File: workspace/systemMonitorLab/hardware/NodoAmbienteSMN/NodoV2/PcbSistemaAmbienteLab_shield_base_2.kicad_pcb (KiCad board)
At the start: 2 copper layers, 55.1 x 66.3 mm, 18 parts, among them J1 Molex_MainBoard_DHT22, J2 Molex_MainBoard_BMP280, J3 Jack-DC, J6 Molex_MainBoard_Led_Status, Q1 Q_NPN_BEC, Q2 Q_NPN_BEC, Q3 Q_NPN_BEC, Q4 Q_NPN_BEC, U1 NodeMcuEsp8266

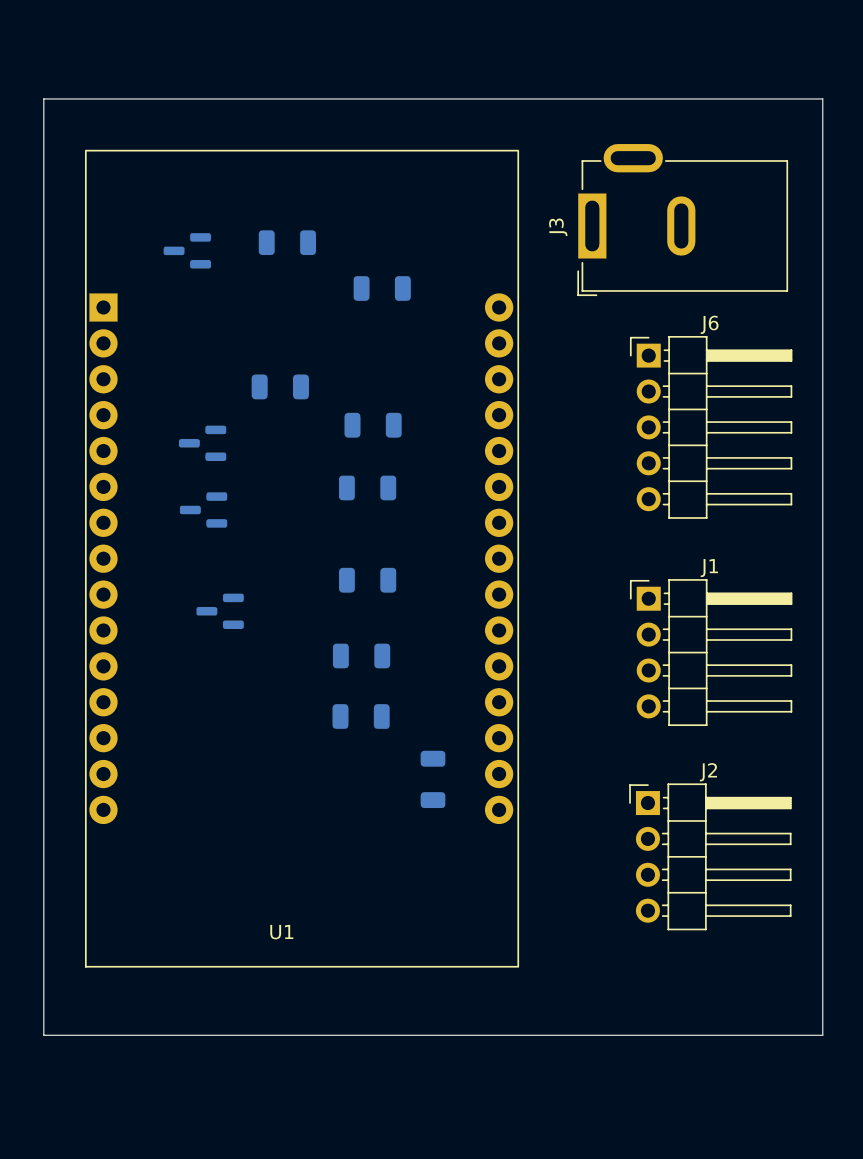
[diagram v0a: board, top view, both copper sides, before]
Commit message: Se termino de generar el diseño de la placa shield_main_board.
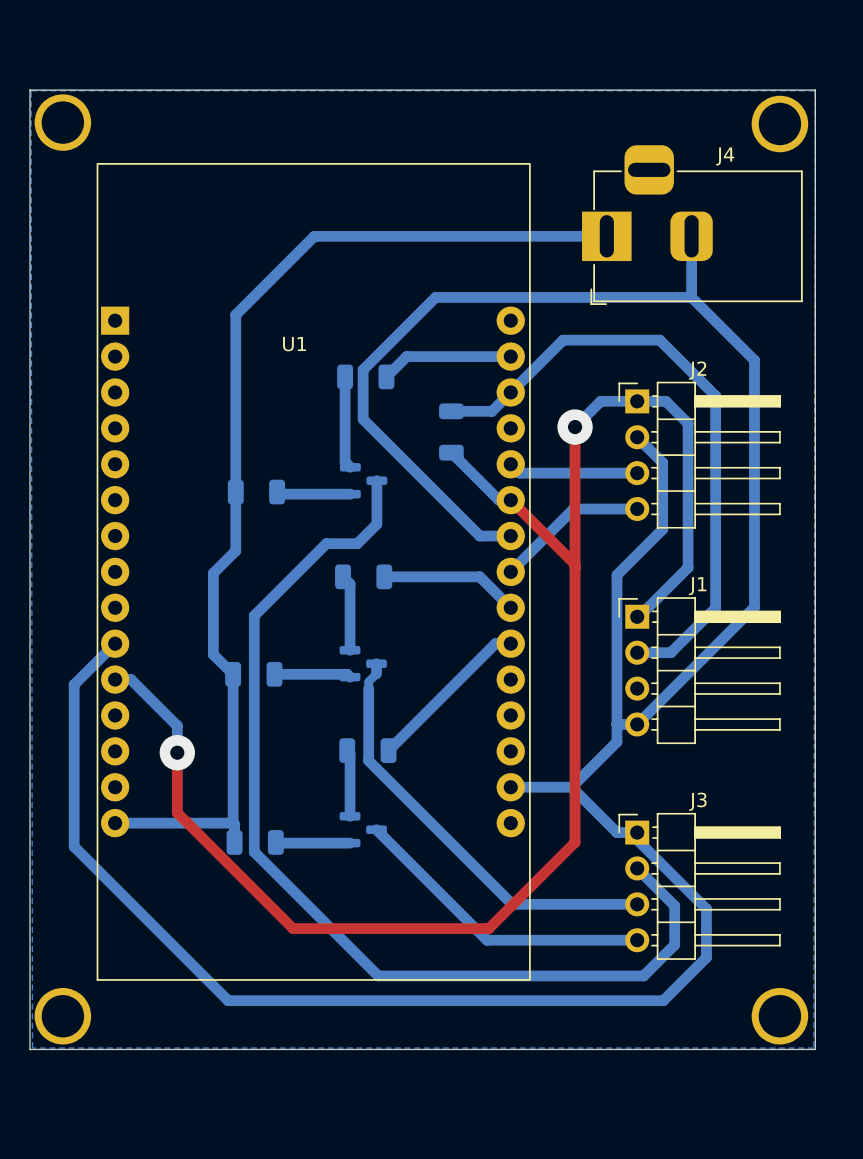
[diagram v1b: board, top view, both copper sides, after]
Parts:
- removed J6: Molex_MainBoard_Led_Status, Connector_PinHeader_2.54mm:PinHeader_1x05_P2.54mm_Horizontal
- removed Q4: Q_NPN_BEC, Package_TO_SOT_SMD:SOT-23
- removed R8, R9: 1k, Resistor_SMD:R_1206_3216Metric
- added ?: , , F.Cu at (117.2, 65.6)
- added ?: , , F.Cu at (117.3, 128.9)
- added ?: , , F.Cu at (168.1, 129.0)
- added ?: , , F.Cu at (168.1, 65.7)
- added J4: Jack-DC, Connector_BarrelJack:BarrelJack_Horizontal, F.Cu at (155.7, 73.7)
- J3: value Jack-DC -> Molex_MainBoard_Led_Status; footprint Connector_BarrelJack:BarrelJack_GCT_DCJ200-10-A_Horizontal -> Connector_PinHeader_2.54mm:PinHeader_1x04_P2.54mm_Horizontal
- Q1, Q2, Q3: value Q_NPN_BEC -> NPN
- R3: value 39 -> 100
- R7: value 39 -> 1k
- U1: footprint NodeMCU_Module:ESP8266_v3 -> Module_commercial:ESP8266_v3
- moved J3 43.0 mm to (157.8, 115.9), turned to 0 degrees
- moved Q3 42.8 mm to (138.5, 115.7), turned to 0 degrees
- moved R6 42.5 mm to (130.8, 116.6)
- moved J2 28.4 mm to (157.8, 85.3)
- moved R1 24.6 mm to (144.7, 87.5), turned to 90 degrees
- moved R7 18.6 mm to (138.8, 110.1), turned to 0 degrees
- moved Q2 15.7 mm to (138.5, 103.9), turned to 0 degrees
- moved Q1 13.7 mm to (138.5, 91.0), turned to 0 degrees
- moved R5 10.5 mm to (130.7, 104.7)
- moved R3 9.52 mm to (130.9, 91.8)
- moved R2 6.09 mm to (138.6, 83.6)
- moved R4 5.60 mm to (138.5, 97.8)
- moved J1 1.52 mm to (157.8, 100.6)
- moved U1 1.25 mm to (133.2, 130.7)
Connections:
- J3 pad 1: +5V -> GND
- J3 pad 2: GND -> Net-(J3-Pin_2)
- J3 pad 3: (no net) -> Net-(J3-Pin_3)
- Q1 pad 1: Net-(Q1-Pad1) -> Net-(Q1-C)
- Q1 pad 2: Net-(Q1-Pad2) -> Net-(Q1-B)
- Q1 pad 3: +5V -> Net-(J3-Pin_2)
- Q2 pad 1: Net-(Q2-Pad1) -> Net-(Q2-C)
- Q2 pad 2: Net-(Q2-Pad2) -> Net-(Q2-B)
- Q2 pad 3: +5V -> Net-(J3-Pin_3)
- Q3 pad 1: Net-(Q3-Pad1) -> Net-(Q3-C)
- Q3 pad 2: Net-(Q3-Pad2) -> Net-(Q3-B)
- Q3 pad 3: +5V -> Net-(J3-Pin_4)
- R2 pad 2: Net-(Q1-Pad1) -> Net-(Q1-B)
- R3 pad 1: Net-(Q1-Pad2) -> Net-(Q1-C)
- R3 pad 2: Net-(J6-Pad2) -> +5V
- R4 pad 2: Net-(Q2-Pad1) -> Net-(Q2-B)
- R5 pad 1: Net-(Q2-Pad2) -> Net-(Q2-C)
- R5 pad 2: Net-(J6-Pad3) -> +5V
- R6 pad 1: Net-(Q3-Pad2) -> Net-(Q3-C)
- R6 pad 2: Net-(J6-Pad4) -> +5V
- R7 pad 1: Net-(Q4-Pad2) -> Net-(Q3-B)
- R7 pad 2: Net-(J6-Pad5) -> /shield_base/LED_DUAL_GREEN
- U1 pad 20: /shield_base/LED_GREEN -> unconnected-(U1-IO15-Pad20)
- U1 pad 25: unconnected-(U1-Pad25) -> 3V3
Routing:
- net GND: track 0.00 -> 199.7 mm
- net 3V3: track 0.00 -> 112.3 mm, vias 0 -> 2
- net +5V: track 0.00 -> 75.5 mm
- net Net-(J3-Pin_2): track 0.00 -> 72.0 mm
- net Net-(J1-Pin_2): track 0.00 -> 44.3 mm
- net Net-(J3-Pin_3): track 0.00 -> 30.3 mm
- net Net-(J3-Pin_4): track 0.00 -> 21.7 mm
- net /shield_base/LED_DUAL_GREEN: track 0.00 -> 11.8 mm
- net /shield_base/SDA: track 0.00 -> 10.8 mm
- net /shield_base/LED_DUAL_RED: track 0.00 -> 9.86 mm
- net /shield_base/LED_YELLOW: track 0.00 -> 9.40 mm
- net /shield_base/SCL: track 0.00 -> 9.21 mm
- net Net-(Q1-B): track 0.00 -> 6.56 mm
- net Net-(Q2-C): track 0.00 -> 5.43 mm
- net Net-(Q2-B): track 0.00 -> 5.41 mm
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- added copper zone on B.Cu, net GND
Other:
- board size 55.1 x 66.3 mm -> 55.6 x 67.9 mm

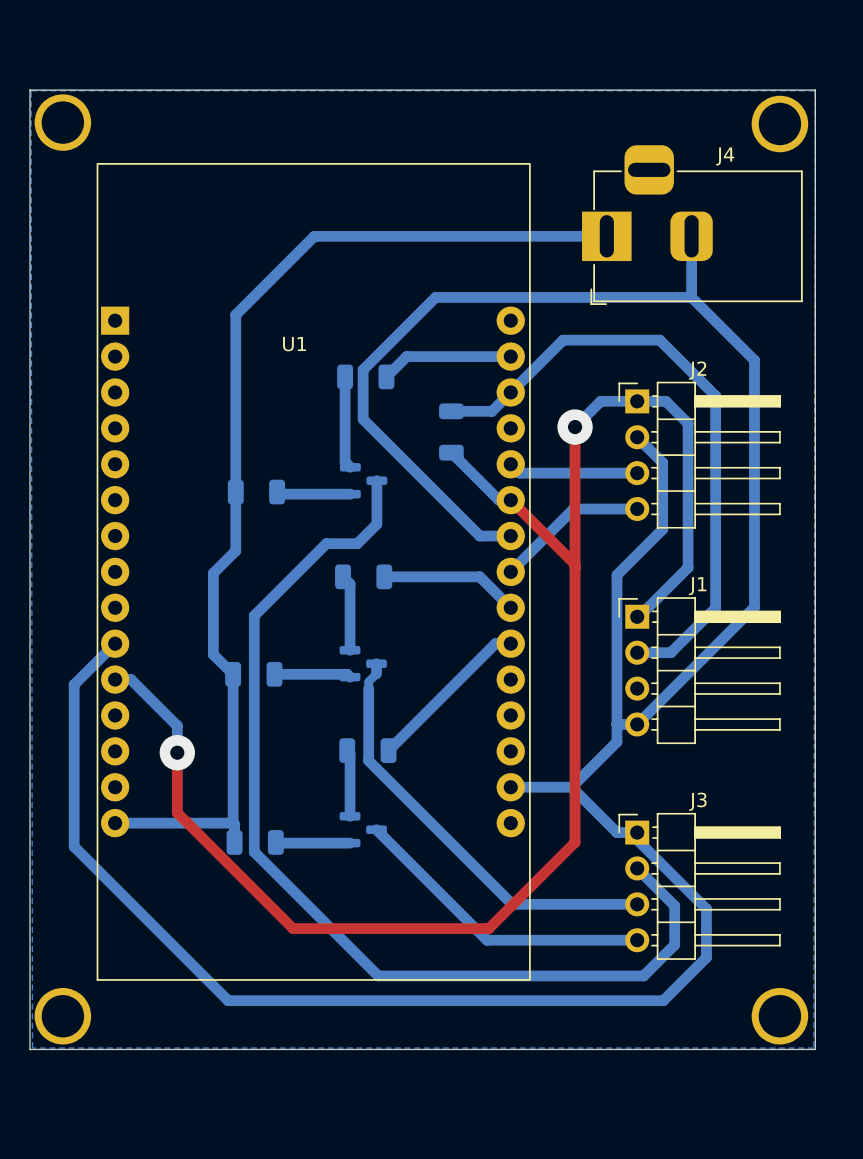
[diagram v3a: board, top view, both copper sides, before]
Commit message: Agregamos el pcb de los Leds, el siguiente paso es ver los conectores Molex comerciales y ajustar el PCB en base a esa dimensiones
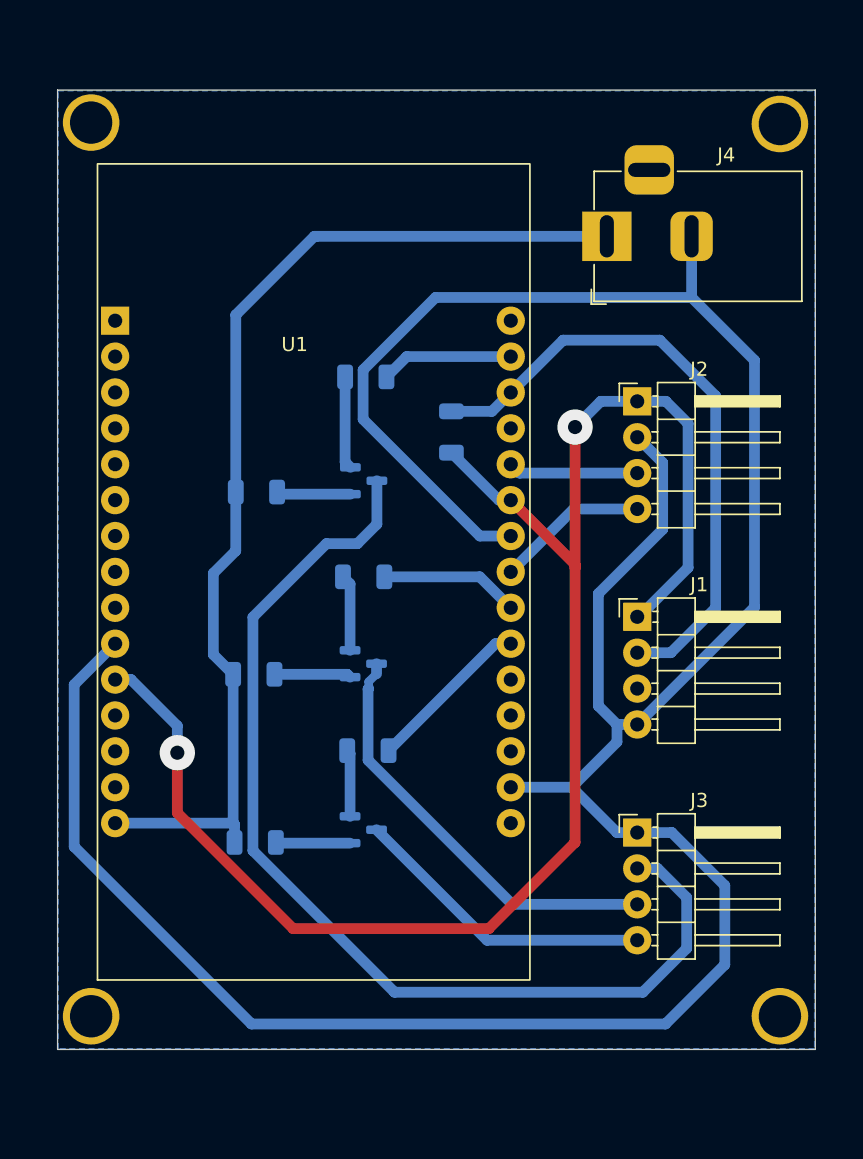
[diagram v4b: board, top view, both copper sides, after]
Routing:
- net GND: track 199.7 -> 206.1 mm
- net Net-(J3-Pin_2): track 72.0 -> 75.2 mm
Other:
- board size 55.6 x 67.9 mm -> 53.6 x 67.9 mm
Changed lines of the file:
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@@
 		(allow_soldermask_bridges_in_footprints no)
 		(tenting front back)
-		(grid_origin 115.85 130.21)
+		(grid_origin 116.825 131.21)
 		(pcbplotparams
 			(layerselection 0x00000000_00000000_55555555_5755f5ff)
@@
 		)
 		(pad "" thru_hole circle
-			(at 0 0 180)
+			(at 2 0 180)
 			(size 4 4)
 			(drill 3)
@@
 		)
 		(pad "" thru_hole circle
-			(at -0.1 0 180)
+			(at 1.9 0 180)
 			(size 4 4)
 			(drill 3)
@@
 		(pad "1" thru_hole rect
 			(at 0 0)
-			(size 1.7 1.7)
+			(size 2 2)
 			(drill 1)
 			(layers "*.Cu" "*.Mask")
@@
 		(pad "2" thru_hole oval
 			(at 0 2.54)
-			(size 1.7 1.7)
+			(size 2 2)
 			(drill 1)
 			(layers "*.Cu" "*.Mask")
@@
 		(pad "3" thru_hole oval
 			(at 0 5.08)
-			(size 1.7 1.7)
+			(size 2 2)
 			(drill 1)
 			(layers "*.Cu" "*.Mask")
@@
 		(pad "4" thru_hole oval
 			(at 0 7.62)
-			(size 1.7 1.7)
+			(size 2 2)
 			(drill 1)
 			(layers "*.Cu" "*.Mask")
@@
 		(pad "1" thru_hole rect
 			(at 0 0)
-			(size 1.7 1.7)
+			(size 2 2)
 			(drill 1)
 			(layers "*.Cu" "*.Mask")
@@
 		(pad "2" thru_hole oval
 			(at 0 2.54)
-			(size 1.7 1.7)
+			(size 2 2)
 			(drill 1)
 			(layers "*.Cu" "*.Mask")
@@
 		(pad "3" thru_hole oval
 			(at 0 5.08)
-			(size 1.7 1.7)
+			(size 2 2)
 			(drill 1)
 			(layers "*.Cu" "*.Mask")
@@
 		(pad "4" thru_hole oval
 			(at 0 7.62)
-			(size 1.7 1.7)
+			(size 2 2)
 			(drill 1)
 			(layers "*.Cu" "*.Mask")
@@
 		(pad "1" thru_hole rect
 			(at 0 0)
-			(size 1.7 1.7)
+			(size 2 2)
 			(drill 1)
 			(layers "*.Cu" "*.Mask")
@@
 		(pad "2" thru_hole oval
 			(at 0 2.54)
-			(size 1.7 1.7)
+			(size 2 2)
 			(drill 1)
 			(layers "*.Cu" "*.Mask")
@@
 		(pad "3" thru_hole oval
 			(at 0 5.08)
-			(size 1.7 1.7)
+			(size 2 2)
 			(drill 1)
 			(layers "*.Cu" "*.Mask")
@@
 		(pad "4" thru_hole oval
 			(at 0 7.62)
-			(size 1.7 1.7)
+			(size 2 2)
 			(drill 1)
 			(layers "*.Cu" "*.Mask")
@@
 		(tags "SOT TO_SOT_SMD")
 		(property "Reference" "Q3"
-			(at 0 2.4 0)
+			(at 0.1875 3.05 0)
 			(layer "B.SilkS")
 			(effects
@@
 	)
 	(gr_rect
-		(start 114.875 63.31)
+		(start 116.825 63.31)
 		(end 170.455 131.21)
 		(stroke
@@
 		(layer "Dwgs.User")
 		(pts
-			(xy 114.875 131.21) (xy 170.455 131.21)
+			(xy 116.825 131.21) (xy 170.455 131.21)
 		)
-		(height 1.75)
+		(height 4.8)
 		(orientation 0)
 		(format
@@
 			(thickness 0.1)
 			(arrow_length 1.27)
-			(text_position_mode 2)
+			(text_position_mode 0)
 			(arrow_direction outward)
 			(extension_height 0.58642)
@@
 			(keep_text_aligned yes)
 		)
-		(gr_text "55.5800 mm"
-			(at 141.1 134.06 0)
+		(gr_text "53.6300 mm"
+			(at 143.64 134.86 0)
 			(layer "Dwgs.User")
 			(effects
@@
 	)
 	(segment
-		(start 156.4173 97.6362)
-		(end 159.65 94.4035)
+		(start 164.05 125.21)
+		(end 164.05 119.61)
 		(width 0.762)
 		(layer "B.Cu")
@@
 	)
 	(segment
-		(start 157.3391 115.86)
-		(end 157.2518 115.86)
+		(start 164.05 119.61)
+		(end 160.3 115.86)
 		(width 0.762)
 		(layer "B.Cu")
@@
 	)
 	(segment
-		(start 159.65 89.68)
-		(end 157.85 87.88)
+		(start 118 116.86)
+		(end 130.55 129.41)
+		(width 0.762)
+		(layer "B.Cu")
+		(net 2)
+	)
+	(segment
+		(start 118 105.3925)
+		(end 118 116.86)
 		(width 0.762)
 		(layer "B.Cu")
@@
 	)
 	(segment
-		(start 118 116.86)
-		(end 128.9 127.76)
+		(start 159.85 129.41)
+		(end 164.05 125.21)
 		(width 0.762)
 		(layer "B.Cu")
@@
 	)
 	(segment
-		(start 156.4173 108.21)
-		(end 156.4173 97.6362)
+		(start 130.55 129.41)
+		(end 159.85 129.41)
 		(width 0.762)
 		(layer "B.Cu")
@@
 	)
 	(segment
-		(start 157.85 108.21)
-		(end 166.15 99.91)
+		(start 120.9 102.4925)
+		(end 118 105.3925)
 		(width 0.762)
 		(layer "B.Cu")
@@
 	)
 	(segment
-		(start 156.4173 109.4454)
-		(end 156.4173 108.21)
+		(start 159.65 89.68)
+		(end 157.85 87.88)
 		(width 0.762)
 		(layer "B.Cu")
@@
 	)
 	(segment
-		(start 138.45 83.1157)
-		(end 138.45 86.61)
+		(start 157.85 108.21)
+		(end 166.15 99.91)
 		(width 0.762)
 		(layer "B.Cu")
@@
 	)
 	(segment
-		(start 162.75 124.71)
-		(end 162.75 121.2709)
+		(start 156.4173 109.4454)
+		(end 156.4173 108.21)
 		(width 0.762)
 		(layer "B.Cu")
@@
 	)
 	(segment
-		(start 128.9 127.76)
-		(end 159.7 127.76)
+		(start 138.45 83.1157)
+		(end 138.45 86.61)
 		(width 0.762)
 		(layer "B.Cu")
@@
 	)
 	(segment
-		(start 118 105.3925)
-		(end 118 116.86)
+		(start 146.7127 94.8727)
+		(end 148.9 94.8727)
 		(width 0.762)
 		(layer "B.Cu")
@@
 	)
 	(segment
-		(start 146.7127 94.8727)
-		(end 148.9 94.8727)
+		(start 157.2518 115.86)
+		(end 156.4173 115.86)
 		(width 0.762)
 		(layer "B.Cu")
@@
 	)
 	(segment
-		(start 157.2518 115.86)
-		(end 156.4173 115.86)
+		(start 156.4173 108.21)
+		(end 155.1 106.8927)
 		(width 0.762)
 		(layer "B.Cu")
@@
 	)
 	(segment
+		(start 155.1 98.9535)
+		(end 159.65 94.4035)
+		(width 0.762)
+		(layer "B.Cu")
+		(net 2)
+	)
+	(segment
 		(start 166.15 99.91)
 		(end 166.15 82.4385)
@@
 	)
 	(segment
-		(start 162.75 121.2709)
-		(end 157.3391 115.86)
+		(start 155.1 106.8927)
+		(end 155.1 98.9535)
 		(width 0.762)
 		(layer "B.Cu")
@@
 	)
 	(segment
-		(start 159.7 127.76)
-		(end 162.75 124.71)
-		(width 0.762)
-		(layer "B.Cu")
-		(net 2)
-	)
-	(segment
-		(start 120.9 102.4925)
-		(end 118 105.3925)
+		(start 160.3 115.86)
+		(end 157.2518 115.86)
 		(width 0.762)
 		(layer "B.Cu")
@@
 	)
 	(segment
-		(start 138.8443 110.7811)
-		(end 138.8443 105.6567)
+		(start 157.85 120.94)
+		(end 149.0032 120.94)
 		(width 0.762)
 		(layer "B.Cu")
@@
 	)
 	(segment
-		(start 157.85 120.94)
-		(end 149.0032 120.94)
+		(start 138.8 105.701)
+		(end 138.8443 105.6567)
 		(width 0.762)
 		(layer "B.Cu")
@@
 	)
 	(segment
-		(start 138.8443 105.6567)
-		(end 138.8443 105.1829)
-		(width 0.601)
+		(start 138.8 110.7368)
+		(end 138.8 105.701)
+		(width 0.762)
 		(layer "B.Cu")
 		(net 3)
@@
 	(segment
 		(start 149.0032 120.94)
-		(end 138.8443 110.7811)
+		(end 138.8 110.7368)
 		(width 0.762)
 		(layer "B.Cu")
@@
 	)
 	(segment
+		(start 138.8443 105.6567)
+		(end 138.8443 105.1829)
+		(width 0.601)
+		(layer "B.Cu")
+		(net 3)
+	)
+	(segment
 		(start 139.4 115.66)
 		(end 147.22 123.48)
@@
 	)
 	(segment
-		(start 130.75 117.2358)
-		(end 130.75 100.5155)
+		(start 161.35 120.46)
+		(end 161.35 124.06)
 		(width 0.762)
 		(layer "B.Cu")
@@
 	)
 	(segment
-		(start 160.5 121.05)
-		(end 160.5 123.81)
+		(start 157.85 118.4)
+		(end 159.29 118.4)
 		(width 0.762)
 		(layer "B.Cu")
@@
 	)
 	(segment
-		(start 135.85275 95.41275)
-		(end 138.04725 95.41275)
+		(start 159.29 118.4)
+		(end 161.35 120.46)
 		(width 0.762)
 		(layer "B.Cu")
@@
 	)
 	(segment
-		(start 139.425 94.035)
-		(end 139.425 90.96)
+		(start 138.04725 95.41275)
+		(end 139.425 94.035)
 		(width 0.762)
 		(layer "B.Cu")
@@
 	)
 	(segment
-		(start 160.5 123.81)
-		(end 158.3 126.01)
+		(start 130.65 100.6155)
+		(end 135.85275 95.41275)
 		(width 0.762)
 		(layer "B.Cu")
@@
 	)
 	(segment
-		(start 158.3 126.01)
-		(end 139.5242 126.01)
+		(start 158.25 127.16)
+		(end 140.6742 127.16)
 		(width 0.762)
 		(layer "B.Cu")
@@
 	)
 	(segment
-		(start 138.04725 95.41275)
-		(end 139.425 94.035)
+		(start 139.425 94.035)
+		(end 139.425 90.96)
 		(width 0.762)
 		(layer "B.Cu")
@@
 	)
 	(segment
-		(start 139.5242 126.01)
-		(end 130.75 117.2358)
+		(start 140.6742 127.16)
+		(end 130.65 117.1358)
 		(width 0.762)
 		(layer "B.Cu")
@@
 	)
 	(segment
-		(start 130.75 100.5155)
-		(end 135.85275 95.41275)
+		(start 130.65 117.1358)
+		(end 130.65 100.6155)
 		(width 0.762)
 		(layer "B.Cu")
@@
 	)
 	(segment
-		(start 157.85 118.4)
-		(end 160.5 121.05)
+		(start 161.35 124.06)
+		(end 158.25 127.16)
+		(width 0.762)
+		(layer "B.Cu")
+		(net 6)
+	)
+	(segment
+		(start 135.85275 95.41275)
+		(end 138.04725 95.41275)
 		(width 0.762)
 		(layer "B.Cu")
@@
 			(clearance 1)
 		)
-		(min_thickness 0.5)
+		(min_thickness 0.25)
 		(filled_areas_thickness no)
 		(fill yes
-			(thermal_gap 0.01)
-			(thermal_bridge_width 2)
+			(thermal_gap 0.5)
+			(thermal_bridge_width 0.5)
 		)
 		(polygon
 			(pts
-				(xy 114.95 63.36) (xy 170.45 63.36) (xy 170.35 131.11) (xy 115.05 131.11)
+				(xy 116.85 63.36) (xy 170.45 63.36) (xy 170.4 131.16) (xy 116.85 131.16)
 			)
 		)

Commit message: Vamos agregando la lista proveedores a la lista de componentes
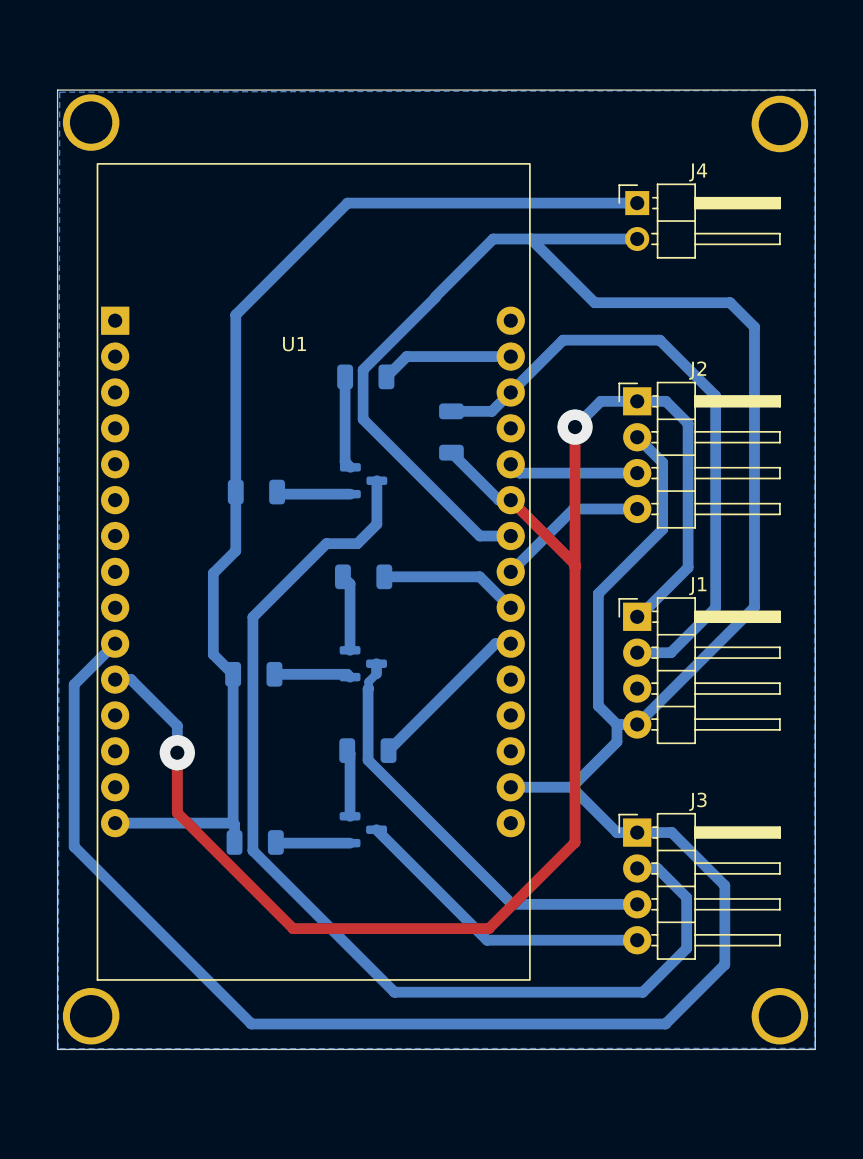
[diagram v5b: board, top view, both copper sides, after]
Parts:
- J4: value Jack-DC -> DC 5V; footprint Connector_BarrelJack:BarrelJack_Horizontal -> Connector_PinHeader_2.54mm:PinHeader_1x02_P2.54mm_Horizontal
- moved J4 3.19 mm to (157.8, 71.3), turned to 0 degrees
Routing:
- net GND: track 206.1 -> 214.1 mm
- net +5V: track 75.5 -> 78.7 mm
